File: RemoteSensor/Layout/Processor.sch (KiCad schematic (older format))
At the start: 18 parts, among them J3 LCD_HEADER, J4 PRG_HEADER, Q3 2N7002, SW2 SW_DPDT_x2, SW3 BTN_LOAD, U7 ESP-12F, U8 LM50CIM3

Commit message: Add an IO expander
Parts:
- removed SW2: SW_DPDT_x2, Switches:SWITCH_DPDT_SMD_AYZ0202, symbol Switch:SW_DPDT_x2
- added R?: R_US, symbol Device:R_US
- added R? (x2): 10k, symbol Device:R_US
- added U?: MCP23008-E_P, digikey-footprints:DIP-18_W7.62mm, symbol dk_Interface-I-O-Expanders:MCP23008-E_P
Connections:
- net labels added: CENTER_BTN, DOWN_BTN, UP_BTN
- net labels removed: SLEEP_PIN
- wire segments 63 -> 81
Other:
- moved on the sheet: J4, R17, R18

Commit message: Assign footprints
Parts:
- R19: renamed from R?; value R_US -> 10k; footprint (none) -> Resistor_SMD:R_0603_1608Metric_Pad1.05x0.95mm_HandSolder
- R20, R21: renamed from R?; footprint (none) -> Resistor_SMD:R_0603_1608Metric_Pad1.05x0.95mm_HandSolder
- U9: renamed from U?; footprint digikey-footprints:DIP-18_W7.62mm -> Package_SO:SOIC-18W_7.5x11.6mm_P1.27mm
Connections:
- net labels added: EXP_RST, SLEEP_PIN, SLEEP_STS
- wire segments 81 -> 83
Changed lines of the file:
@@
 	6200 2650 6550 2650
-Wire Wire Line
-	6200 2750 6550 2750
 Wire Wire Line
 	6200 2950 6550 2950
@@
 Connection ~ 5650 5350
 $Comp
-L SparkFun-PowerSymbols:3.3V #SUPPLY?
+L SparkFun-PowerSymbols:3.3V #SUPPLY0120
 U 1 1 5EF03A19
 P 6200 4000
-F 0 "#SUPPLY?" H 6250 4000 45  0001 L BNN
+F 0 "#SUPPLY0120" H 6250 4000 45  0001 L BNN
 F 1 "3.3V" H 6200 4276 45  0000 C CNN
 F 2 "XXX-00000" H 6200 4181 60  0000 C CNN
@@
 	6200 4000 6200 4050
 $Comp
-L dk_Interface-I-O-Expanders:MCP23008-E_P U?
+L dk_Interface-I-O-Expanders:MCP23008-E_P U9
 U 1 1 5EEF9F80
 P 6300 4750
-F 0 "U?" H 6650 5500 60  0000 C CNN
+F 0 "U9" H 6650 5500 60  0000 C CNN
 F 1 "MCP23008-E_P" H 6650 5400 60  0000 C CNN
-F 2 "digikey-footprints:DIP-18_W7.62mm" H 6500 4950 60  0001 L CNN
+F 2 "Package_SO:SOIC-18W_7.5x11.6mm_P1.27mm" H 6500 4950 60  0001 L CNN
 F 3 "http://www.microchip.com/mymicrochip/filehandler.aspx?ddocname=en021920" H 6500 5050 60  0001 L CNN
 F 4 "MCP23008-E/P-ND" H 6500 5150 60  0001 L CNN "Digi-Key_PN"
@@
 $EndComp
 $Comp
-L SparkFun-PowerSymbols:GND #GND?
+L SparkFun-PowerSymbols:GND #GND0122
 U 1 1 5EF09AEA
 P 6300 5900
-F 0 "#GND?" H 6350 5850 45  0001 L BNN
+F 0 "#GND0122" H 6350 5850 45  0001 L BNN
 F 1 "GND" H 6300 5730 45  0000 C CNN
 F 2 "" H 6300 5800 60  0001 C CNN
@@
 	5400 5050 5800 5050
 $Comp
-L Device:R_US R?
+L Device:R_US R19
 U 1 1 5EF1D3A2
 P 5000 5400
-F 0 "R?" H 5068 5446 50  0000 L CNN
-F 1 "R_US" H 5068 5355 50  0000 L CNN
-F 2 "" V 5040 5390 50  0001 C CNN
+F 0 "R19" H 5068 5446 50  0000 L CNN
+F 1 "10k" H 5068 5355 50  0000 L CNN
+F 2 "Resistor_SMD:R_0603_1608Metric_Pad1.05x0.95mm_HandSolder" V 5040 5390 50  0001 C CNN
 F 3 "~" H 5000 5400 50  0001 C CNN
 	1    5000 5400
@@
 	5000 5550 5800 5550
 $Comp
-L SparkFun-PowerSymbols:3.3V #SUPPLY?
+L SparkFun-PowerSymbols:3.3V #SUPPLY0121
 U 1 1 5EF20521
 P 5000 5250
-F 0 "#SUPPLY?" H 5050 5250 45  0001 L BNN
-F 1 "3.3V" H 5000 5526 45  0000 C CNN
-F 2 "XXX-00000" H 5000 5431 60  0000 C CNN
+F 0 "#SUPPLY0121" H 5050 5250 45  0001 L BNN
+F 1 "3.3V" H 4700 5350 45  0000 C CNN
+F 2 "XXX-00000" H 4700 5250 60  0000 C CNN
 F 3 "" H 5000 5250 60  0001 C CNN
 	1    5000 5250
@@
 $EndComp
 $Comp
-L Device:R_US R?
+L Device:R_US R20
 U 1 1 5EF20C41
 P 7000 1650
-F 0 "R?" H 7068 1696 50  0000 L CNN
+F 0 "R20" H 7068 1696 50  0000 L CNN
 F 1 "10k" H 7068 1605 50  0000 L CNN
-F 2 "" V 7040 1640 50  0001 C CNN
+F 2 "Resistor_SMD:R_0603_1608Metric_Pad1.05x0.95mm_HandSolder" V 7040 1640 50  0001 C CNN
 F 3 "~" H 7000 1650 50  0001 C CNN
 	1    7000 1650
@@
 	6200 2150 7000 2150
 $Comp
-L Device:R_US R?
+L Device:R_US R21
 U 1 1 5EF266EA
 P 7000 3000
-F 0 "R?" H 7068 3046 50  0000 L CNN
+F 0 "R21" H 7068 3046 50  0000 L CNN
 F 1 "10k" H 7068 2955 50  0000 L CNN
-F 2 "" V 7040 2990 50  0001 C CNN
+F 2 "Resistor_SMD:R_0603_1608Metric_Pad1.05x0.95mm_HandSolder" V 7040 2990 50  0001 C CNN
 F 3 "~" H 7000 3000 50  0001 C CNN
 	1    7000 3000
@@
 Text GLabel 6550 2450 2    50   Input ~ 0
 BATT_PIN
+Text GLabel 6550 2550 2    50   Input ~ 0
+SLEEP_PIN
+Text GLabel 5300 4850 0    50   Input ~ 0
+SLEEP_STS
+Text GLabel 5300 4950 0    50   Input ~ 0
+WAKE_STS
+Wire Wire Line
+	5300 4850 5800 4850
+Wire Wire Line
+	5300 4950 5800 4950
+Text GLabel 6550 2650 2    50   Input ~ 0
+EXP_RST
+Text GLabel 4700 5550 0    50   Input ~ 0
+EXP_RST
+Wire Wire Line
+	4700 5550 5000 5550
+Connection ~ 5000 5550
 $EndSCHEMATC

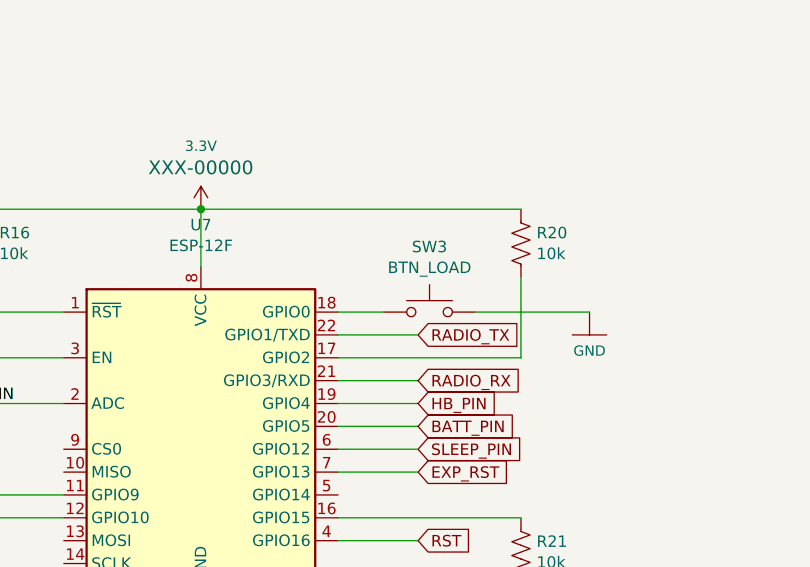
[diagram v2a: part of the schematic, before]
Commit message: Add FTDI USB to serial
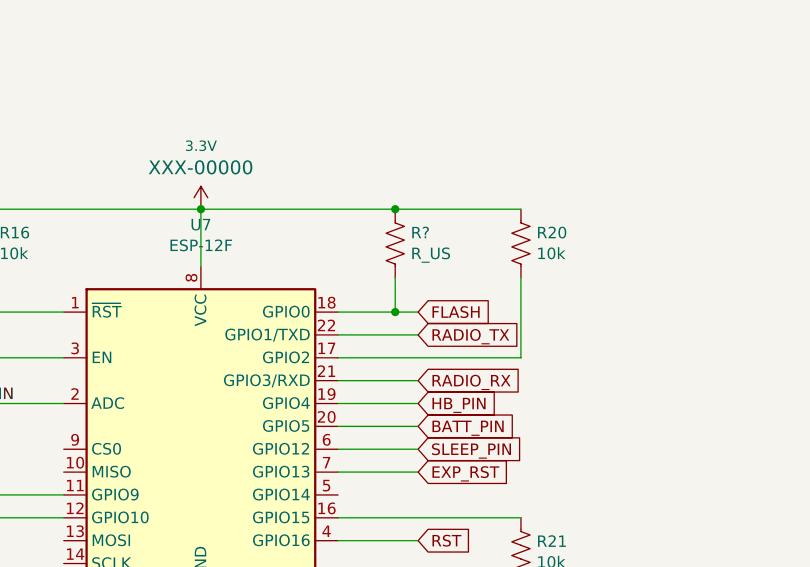
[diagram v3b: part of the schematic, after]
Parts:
- removed SW3: BTN_LOAD, Button_Switch_SMD:SW_SPST_TL3342, symbol Switch:SW_Push
- added R?: R_US, symbol Device:R_US
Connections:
- net labels added: FLASH
- wire segments 83 -> 85
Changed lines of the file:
@@
 $Descr A4 11693 8268
 encoding utf-8
-Sheet 4 4
+Sheet 4 5
 Title ""
 Date ""
@@
 Wire Wire Line
 	5000 2750 4250 2750
-Wire Wire Line
-	6800 1950 7300 1950
 Text Label 4450 2350 0    50   ~ 0
 TEMP_PIN
 Wire Wire Line
 	5000 2350 4450 2350
-$Comp
-L Switch:SW_Push SW?
-U 1 1 5EF69116
-P 6600 1950
-AR Path="/5EF69116" Ref="SW?"  Part="1"
-AR Path="/5EF5F91F/5EF69116" Ref="SW3"  Part="1"
-F 0 "SW3" H 6600 2235 50  0000 C CNN
-F 1 "BTN_LOAD" H 6600 2144 50  0000 C CNN
-F 2 "Button_Switch_SMD:SW_SPST_TL3342" H 6600 2150 50  0001 C CNN
-F 3 "~" H 6600 2150 50  0001 C CNN
-	1    6600 1950
-	1    0    0    -1
-$EndComp
 $Comp
 L SparkFun-PowerSymbols:3.3V #SUPPLY?
@@
 	1    0    0    -1
 $EndComp
-$Comp
-L SparkFun-PowerSymbols:GND #GND?
-U 1 1 5EF69122
-P 7300 1950
-AR Path="/5EF69122" Ref="#GND?"  Part="1"
-AR Path="/5EF5F91F/5EF69122" Ref="#GND0113"  Part="1"
-F 0 "#GND0113" H 7350 1900 45  0001 L BNN
-F 1 "GND" H 7300 1780 45  0000 C CNN
-F 2 "" H 7300 1850 60  0001 C CNN
-F 3 "" H 7300 1850 60  0001 C CNN
-	1    7300 1950
-	1    0    0    -1
-$EndComp
-Wire Wire Line
-	6200 1950 6400 1950
 Connection ~ 5600 1500
 Wire Wire Line
@@
 $EndComp
 Wire Wire Line
-	5600 1500 7000 1500
-Wire Wire Line
 	7000 1800 7000 2150
 Wire Wire Line
@@
 	4700 5550 5000 5550
 Connection ~ 5000 5550
+Wire Wire Line
+	5600 1500 6450 1500
+$Comp
+L Device:R_US R?
+U 1 1 5EF17614
+P 6450 1650
+F 0 "R?" H 6518 1696 50  0000 L CNN
+F 1 "R_US" H 6518 1605 50  0000 L CNN
+F 2 "" V 6490 1640 50  0001 C CNN
+F 3 "~" H 6450 1650 50  0001 C CNN
+	1    6450 1650
+	1    0    0    -1
+$EndComp
+Connection ~ 6450 1500
+Wire Wire Line
+	6450 1500 7000 1500
+Wire Wire Line
+	6450 1800 6450 1950
+Wire Wire Line
+	6200 1950 6450 1950
+Wire Wire Line
+	6450 1950 6550 1950
+Connection ~ 6450 1950
+Text GLabel 6550 1950 2    50   Input ~ 0
+FLASH
 $EndSCHEMATC

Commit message: Update sensor schematic
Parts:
- Q3: symbol dk_Transistors-FETs-MOSFETs-Single:2N7002 -> RemoteSensor-rescue:2N7002-dk_Transistors-FETs-MOSFETs-Single
- S1: symbol SparkFun-Switches:NAV_SWITCH -> RemoteSensor-rescue:NAV_SWITCH-SparkFun-Switches
- U8: symbol LM50CIM3:LM50CIM3 -> RemoteSensor-rescue:LM50CIM3-LM50CIM3
- U9: symbol dk_Interface-I-O-Expanders:MCP23008-E_P -> RemoteSensor-rescue:MCP23008-E_P-dk_Interface-I-O-Expanders
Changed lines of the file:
@@
 EESchema Schematic File Version 4
-LIBS:RemoteSensor-cache
-EELAYER 29 0
+EELAYER 30 0
 EELAYER END
 $Descr A4 11693 8268
@@
 	5000 2350 4450 2350
 $Comp
-L SparkFun-PowerSymbols:3.3V #SUPPLY?
+L RemoteSensor-rescue:3.3V-SparkFun-PowerSymbols #SUPPLY?
 U 1 1 5EF6911C
 P 5600 1500
@@
 $EndComp
 $Comp
-L SparkFun-PowerSymbols:GND #GND?
+L RemoteSensor-rescue:GND-SparkFun-PowerSymbols #GND?
 U 1 1 5EF69140
 P 5600 3250
@@
 $EndComp
 $Comp
-L SparkFun-Switches:NAV_SWITCH S?
+L RemoteSensor-rescue:NAV_SWITCH-SparkFun-Switches S?
 U 1 1 5EF6B1EF
 P 9500 1200
@@
 $EndComp
 $Comp
-L SparkFun-PowerSymbols:GND #GND?
+L RemoteSensor-rescue:GND-SparkFun-PowerSymbols #GND?
 U 1 1 5EF6B1F5
 P 9900 1200
@@
 $EndComp
 $Comp
-L SparkFun-PowerSymbols:3.3V #SUPPLY?
+L RemoteSensor-rescue:3.3V-SparkFun-PowerSymbols #SUPPLY?
 U 1 1 5EF6D225
 P 2050 1500
@@
 $EndComp
 $Comp
-L SparkFun-PowerSymbols:3.3V #SUPPLY?
+L RemoteSensor-rescue:3.3V-SparkFun-PowerSymbols #SUPPLY?
 U 1 1 5EF6FC22
 P 2250 3100
@@
 SDA
 $Comp
-L SparkFun-PowerSymbols:GND #GND?
+L RemoteSensor-rescue:GND-SparkFun-PowerSymbols #GND?
 U 1 1 5EF6FC2F
 P 2250 3900
@@
 $EndComp
 $Comp
-L dk_Transistors-FETs-MOSFETs-Single:2N7002 Q?
+L RemoteSensor-rescue:2N7002-dk_Transistors-FETs-MOSFETs-Single Q?
 U 1 1 5EF6FC40
 P 2250 3700
@@
 $EndComp
 $Comp
-L LM50CIM3:LM50CIM3 U?
+L RemoteSensor-rescue:LM50CIM3-LM50CIM3 U?
 U 1 1 5EF73CDC
 P 9450 2550
@@
 $EndComp
 $Comp
-L SparkFun-PowerSymbols:3.3V #SUPPLY?
+L RemoteSensor-rescue:3.3V-SparkFun-PowerSymbols #SUPPLY?
 U 1 1 5EF73CE2
 P 8750 2350
@@
 	8750 2550 8750 2350
 $Comp
-L SparkFun-PowerSymbols:GND #GND?
+L RemoteSensor-rescue:GND-SparkFun-PowerSymbols #GND?
 U 1 1 5EF73CE9
 P 8750 3150
@@
 $EndComp
 $Comp
-L SparkFun-PowerSymbols:GND #GND?
+L RemoteSensor-rescue:GND-SparkFun-PowerSymbols #GND?
 U 1 1 5EF7CD1C
 P 9500 5200
@@
 	3000 5550 2800 5550
 $Comp
-L SparkFun-PowerSymbols:GND #GND?
+L RemoteSensor-rescue:GND-SparkFun-PowerSymbols #GND?
 U 1 1 5EF7FA2C
 P 3000 5650
@@
 Connection ~ 5650 5350
 $Comp
-L SparkFun-PowerSymbols:3.3V #SUPPLY0120
+L RemoteSensor-rescue:3.3V-SparkFun-PowerSymbols #SUPPLY0120
 U 1 1 5EF03A19
 P 6200 4000
@@
 	6200 4000 6200 4050
 $Comp
-L dk_Interface-I-O-Expanders:MCP23008-E_P U9
+L RemoteSensor-rescue:MCP23008-E_P-dk_Interface-I-O-Expanders U9
 U 1 1 5EEF9F80
 P 6300 4750
@@
 $EndComp
 $Comp
-L SparkFun-PowerSymbols:GND #GND0122
+L RemoteSensor-rescue:GND-SparkFun-PowerSymbols #GND0122
 U 1 1 5EF09AEA
 P 6300 5900
@@
 	5000 5550 5800 5550
 $Comp
-L SparkFun-PowerSymbols:3.3V #SUPPLY0121
+L RemoteSensor-rescue:3.3V-SparkFun-PowerSymbols #SUPPLY0121
 U 1 1 5EF20521
 P 5000 5250

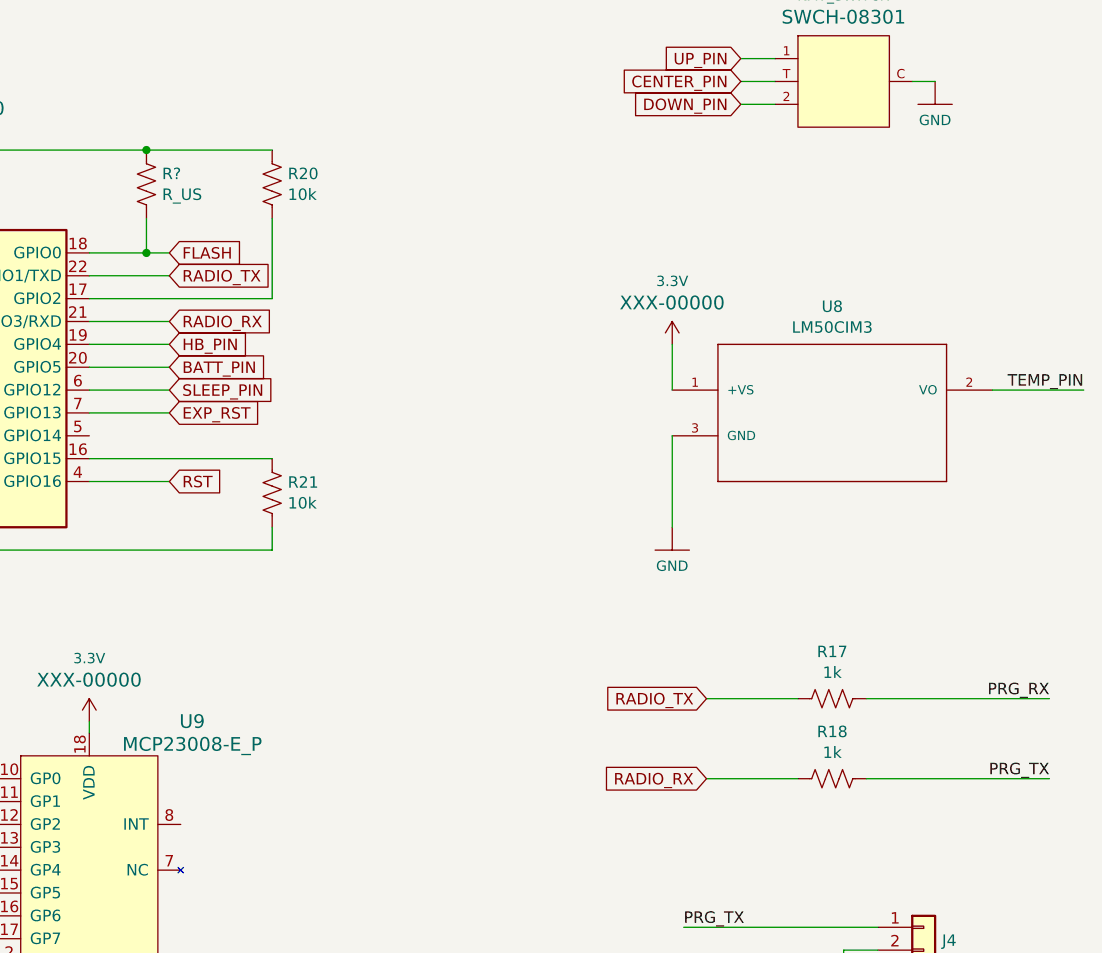
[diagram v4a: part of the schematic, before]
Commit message: Add footprints and component values
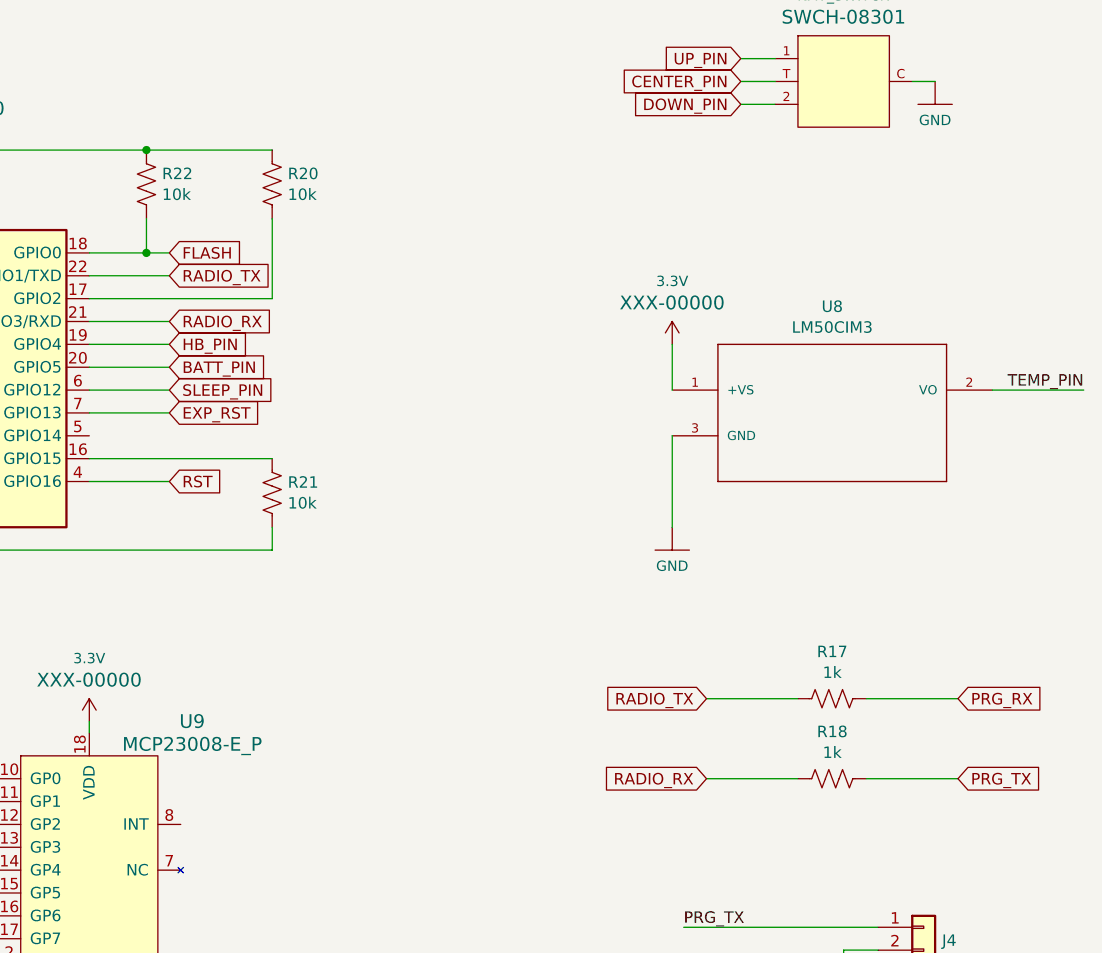
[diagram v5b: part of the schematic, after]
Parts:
- R22: renamed from R?; value R_US -> 10k; footprint (none) -> Resistor_SMD:R_0603_1608Metric_Pad1.05x0.95mm_HandSolder
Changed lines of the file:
@@
 	0    1    1    0
 $EndComp
-Text Label 10400 3900 2    50   ~ 0
-PRG_RX
-Text Label 10400 4250 2    50   ~ 0
-PRG_TX
-Wire Wire Line
-	9600 4250 10400 4250
-Wire Wire Line
-	9600 3900 10400 3900
 $Comp
 L Device:LED D?
@@
 	5600 1500 6450 1500
 $Comp
-L Device:R_US R?
+L Device:R_US R22
 U 1 1 5EF17614
 P 6450 1650
-F 0 "R?" H 6518 1696 50  0000 L CNN
-F 1 "R_US" H 6518 1605 50  0000 L CNN
-F 2 "" V 6490 1640 50  0001 C CNN
+F 0 "R22" H 6518 1696 50  0000 L CNN
+F 1 "10k" H 6518 1605 50  0000 L CNN
+F 2 "Resistor_SMD:R_0603_1608Metric_Pad1.05x0.95mm_HandSolder" V 6490 1640 50  0001 C CNN
 F 3 "~" H 6450 1650 50  0001 C CNN
 	1    6450 1650
@@
 Text GLabel 6550 1950 2    50   Input ~ 0
 FLASH
+Text GLabel 10000 3900 2    50   Input ~ 0
+PRG_RX
+Text GLabel 10000 4250 2    50   Input ~ 0
+PRG_TX
+Wire Wire Line
+	9600 3900 10000 3900
+Wire Wire Line
+	9600 4250 10000 4250
 $EndSCHEMATC

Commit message: Edit layout
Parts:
- added SW?: SW_Push, Button_Switch_SMD:SW_SPST_TL3342, symbol Switch:SW_Push
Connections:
- net CENTER_PIN is gone; now on net CENTER_BTN: S1.T
- net DOWN_PIN is gone; now on net DOWN_BTN: S1.2
- net UP_PIN is gone; now on net UP_BTN: S1.1
- net FLASH: now also SW?.1
- net GND: now also SW?.2
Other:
- moved on the sheet: D1, D2, J3, Q3, R11, R12, R13, R14
